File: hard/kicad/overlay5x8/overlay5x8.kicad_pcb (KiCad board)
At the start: 2 copper layers, 142.2 x 53.3 mm, 41 parts, among them SW1 1 !, SW10 0 _, SW11 Q ¡, SW12 W ~~, SW13 E é, SW14 R <, SW15 T >, SW16 Y ü, SW17 U ú, SW18 I í, SW19 O ó, SW2 2 @, SW20 P ", SW22 S ;, SW23 D |, SW24 F [, SW25 G ], SW26 H ^, SW27 J -, SW28 K +, SW29 L =, SW3 3 #, SW30 ENTER ñ, SW33 X ¿, SW34 C ?, SW35 V /, SW36 B *, SW37 N ,, SW38 M ., SW39 ALT, SW4 4 $, SW40 SPACE, SW5 5 %, SW6 6 &, SW7 7 ', SW8 8 (, SW9 9 )

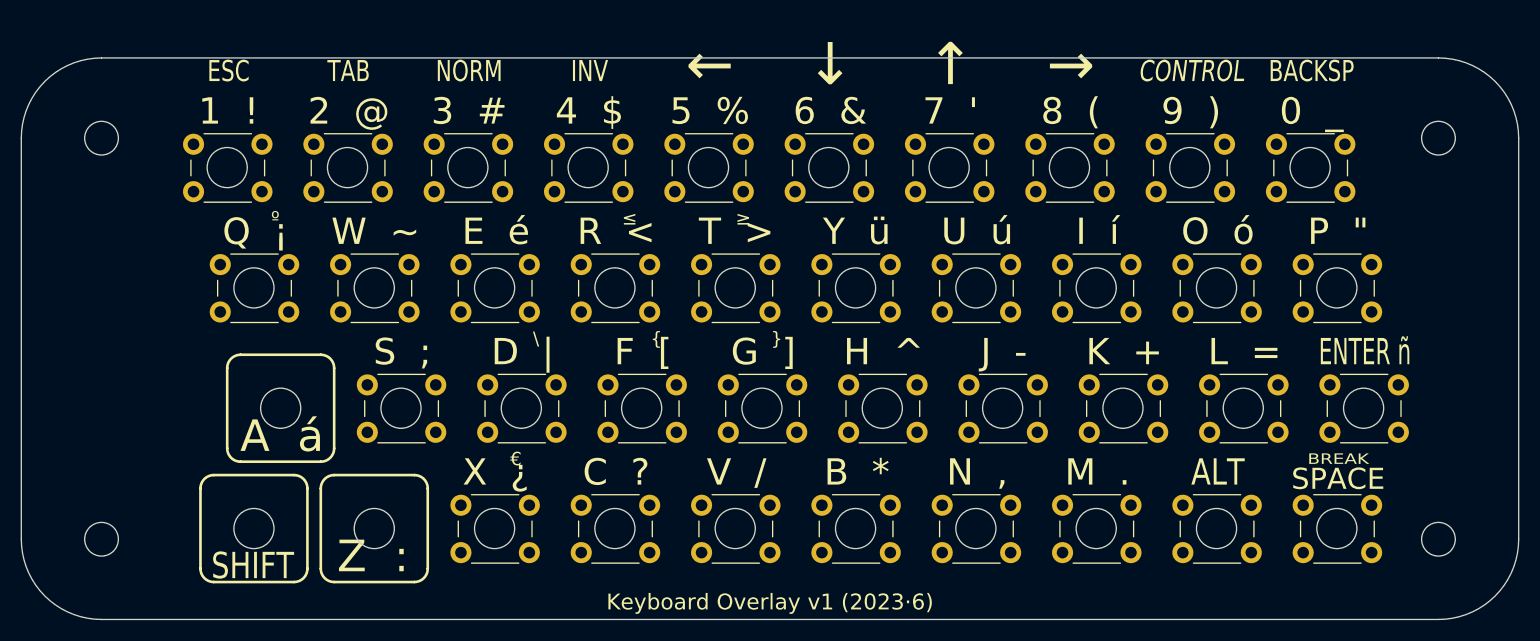
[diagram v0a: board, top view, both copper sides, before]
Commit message: finish keyboard overlay
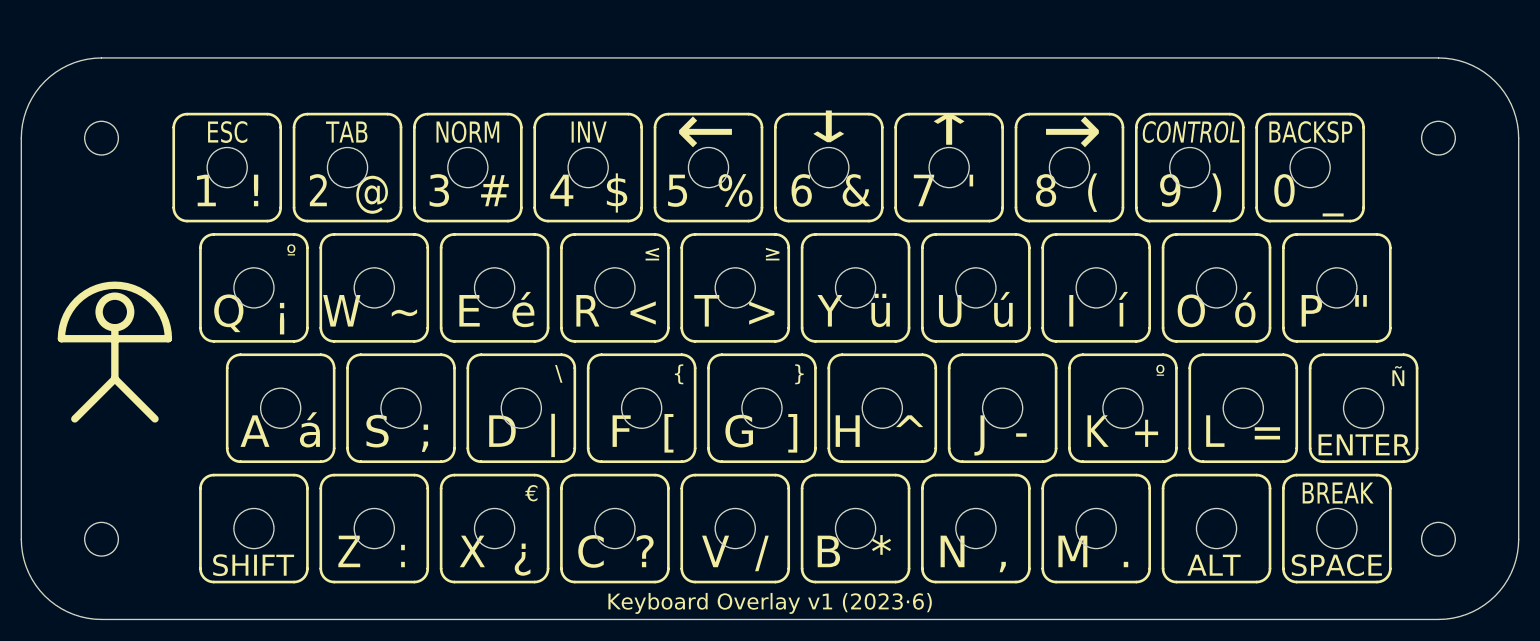
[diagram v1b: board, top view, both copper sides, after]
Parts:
- removed SW1: 1 !, Button_Switch_THT:SW_PUSH_6mm
- removed SW10: 0 _, Button_Switch_THT:SW_PUSH_6mm
- removed SW11: Q ¡, Button_Switch_THT:SW_PUSH_6mm
- removed SW12: W ~~, Button_Switch_THT:SW_PUSH_6mm
- removed SW13: E é, Button_Switch_THT:SW_PUSH_6mm
- removed SW14: R <, Button_Switch_THT:SW_PUSH_6mm
- removed SW15: T >, Button_Switch_THT:SW_PUSH_6mm
- removed SW16: Y ü, Button_Switch_THT:SW_PUSH_6mm
- removed SW17: U ú, Button_Switch_THT:SW_PUSH_6mm
- removed SW18: I í, Button_Switch_THT:SW_PUSH_6mm
- removed SW19: O ó, Button_Switch_THT:SW_PUSH_6mm
- removed SW2: 2 @, Button_Switch_THT:SW_PUSH_6mm
- removed SW20: P ", Button_Switch_THT:SW_PUSH_6mm
- removed SW22: S ;, Button_Switch_THT:SW_PUSH_6mm
- removed SW23: D |, Button_Switch_THT:SW_PUSH_6mm
- removed SW24: F [, Button_Switch_THT:SW_PUSH_6mm
- removed SW25: G ], Button_Switch_THT:SW_PUSH_6mm
- removed SW26: H ^, Button_Switch_THT:SW_PUSH_6mm
- removed SW27: J -, Button_Switch_THT:SW_PUSH_6mm
- removed SW28: K +, Button_Switch_THT:SW_PUSH_6mm
- removed SW29: L =, Button_Switch_THT:SW_PUSH_6mm
- removed SW3: 3 #, Button_Switch_THT:SW_PUSH_6mm
- removed SW30: ENTER ñ, Button_Switch_THT:SW_PUSH_6mm
- removed SW33: X ¿, Button_Switch_THT:SW_PUSH_6mm
- removed SW34: C ?, Button_Switch_THT:SW_PUSH_6mm
- removed SW35: V /, Button_Switch_THT:SW_PUSH_6mm
- removed SW36: B *, Button_Switch_THT:SW_PUSH_6mm
- removed SW37: N ,, Button_Switch_THT:SW_PUSH_6mm
- removed SW38: M ., Button_Switch_THT:SW_PUSH_6mm
- removed SW39: ALT, Button_Switch_THT:SW_PUSH_6mm
- removed SW4: 4 $, Button_Switch_THT:SW_PUSH_6mm
- removed SW40: SPACE, Button_Switch_THT:SW_PUSH_6mm
- removed SW5: 5 %, Button_Switch_THT:SW_PUSH_6mm
- removed SW6: 6 &, Button_Switch_THT:SW_PUSH_6mm
- removed SW7: 7 ', Button_Switch_THT:SW_PUSH_6mm
- removed SW8: 8 (, Button_Switch_THT:SW_PUSH_6mm
- removed SW9: 9 ), Button_Switch_THT:SW_PUSH_6mm
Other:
- board text added: "0 _"
- board text added: "1 !"
- board text added: "2 @"
- board text added: "3 #"
- board text added: "4 $"
- board text added: "5 %"
- board text added: "6 &"
- board text added: "7 '"
- board text added: "8 ("
- board text added: "9 )"
- board text added: "ALT"
- board text added: "B *"
- board text added: "BACKSP"
- board text added: "BREAK"
- board text added: "C ?"
- board text added: "CONTROL"
- board text added: "D |"
- board text added: "E é"
- board text added: "ENTER"
- board text added: "ESC"
- board text added: "F ["
- board text added: "G ]"
- board text added: "H ^"
- board text added: "I í"
- board text added: "INV"
- board text added: "J -"
- board text added: "K +"
- board text added: "L ="
- board text added: "M ."
- board text added: "N ,"
- board text added: "NORM"
- board text added: "O ó"
- board text added: "P ""
- board text added: "Q ¡"
- board text added: "R <"
- board text added: "S ;"
- board text added: "SPACE"
- board text added: "T >"
- board text added: "TAB"
- board text added: "U ú"
- board text added: "V /"
- board text added: "W ~~"
- board text added: "X ¿"
- board text added: "Y ü"
- board text added: "\"
- board text added: "{"
- board text added: "}"
- board text added: "º"
- board text added: "Ñ"
- board text added: "€"
- board text added: "←"
- board text added: "↑"
- board text added: "→"
- board text added: "↓"
- board text added: "≤"
- board text added: "≥"

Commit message: add copper planes to overlay
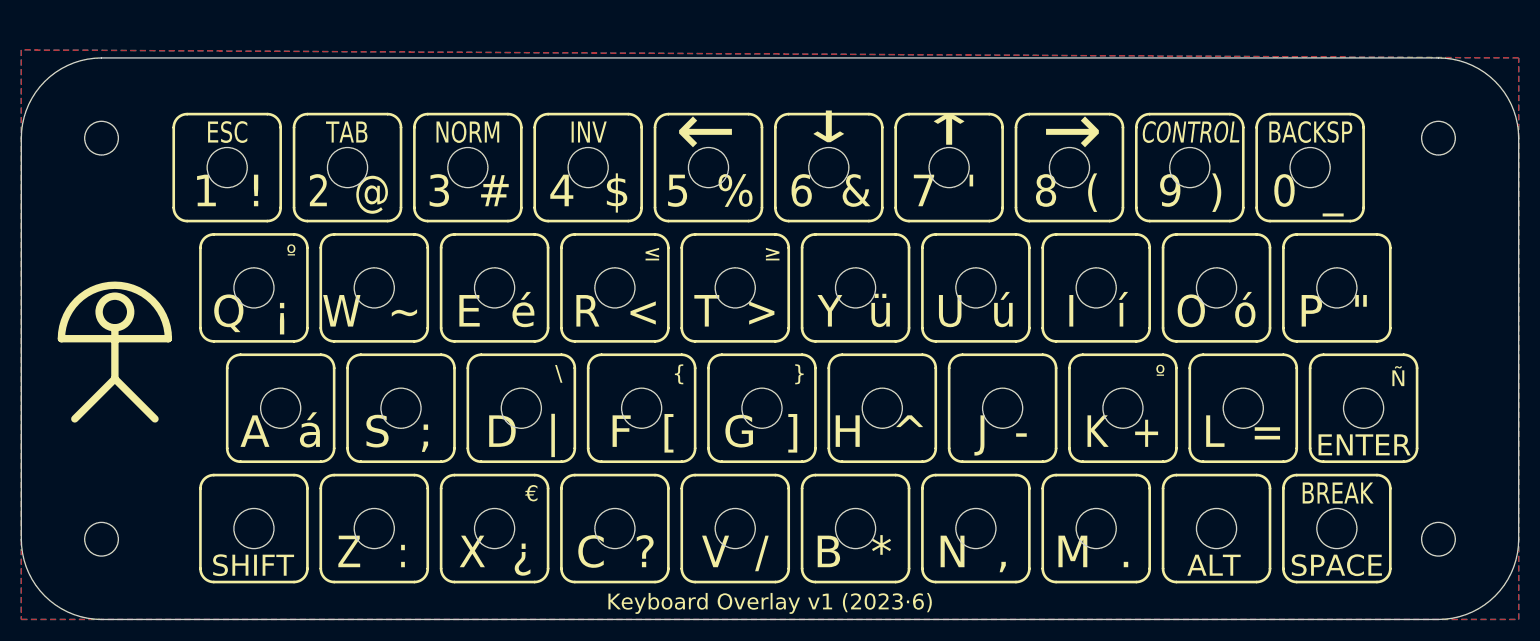
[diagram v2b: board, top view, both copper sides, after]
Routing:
- added copper zone on B.Cu, net (none)
- added copper zone on F.Cu, net (none)
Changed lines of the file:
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@@
     (effects (font (size 2.54 2.54) (thickness 0.45)) (justify mirror))
   )
+  (zone (net 0) (net_name "") (layer F.Cu) (hatch edge 0.508)
+    (connect_pads (clearance 0.508))
+    (min_thickness 0.254)
+    (fill yes (arc_segments 32) (thermal_gap 0.508) (thermal_bridge_width 0.508))
+    (polygon
+      (pts
+        (xy 34.29 79.248) (xy 34.29 133.35) (xy 176.53 133.35) (xy 176.53 80.01)
+      )
+    )
+  )
+  (zone (net 0) (net_name "") (layer B.Cu) (hatch edge 0.508)
+    (connect_pads (clearance 0.508))
+    (min_thickness 0.254)
+    (fill yes (arc_segments 32) (thermal_gap 0.508) (thermal_bridge_width 0.508))
+    (polygon
+      (pts
+        (xy 34.29 79.248) (xy 34.29 133.35) (xy 176.53 133.35) (xy 176.53 80.01)
+      )
+    )
+  )
 )
